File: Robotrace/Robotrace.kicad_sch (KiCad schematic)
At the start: 36 parts, among them J1 USB_C_Receptacle_USB2.0_16P, J10 Side_L, J6 STDC14, J7 Conn_02x05_Odd_Even, J8 Conn_02x05_Odd_Even, J9 Side_R, Q5 BSS138, SW1 SW_DPDT_x2, U1 STM32F469VGTx, Y1 8MHz

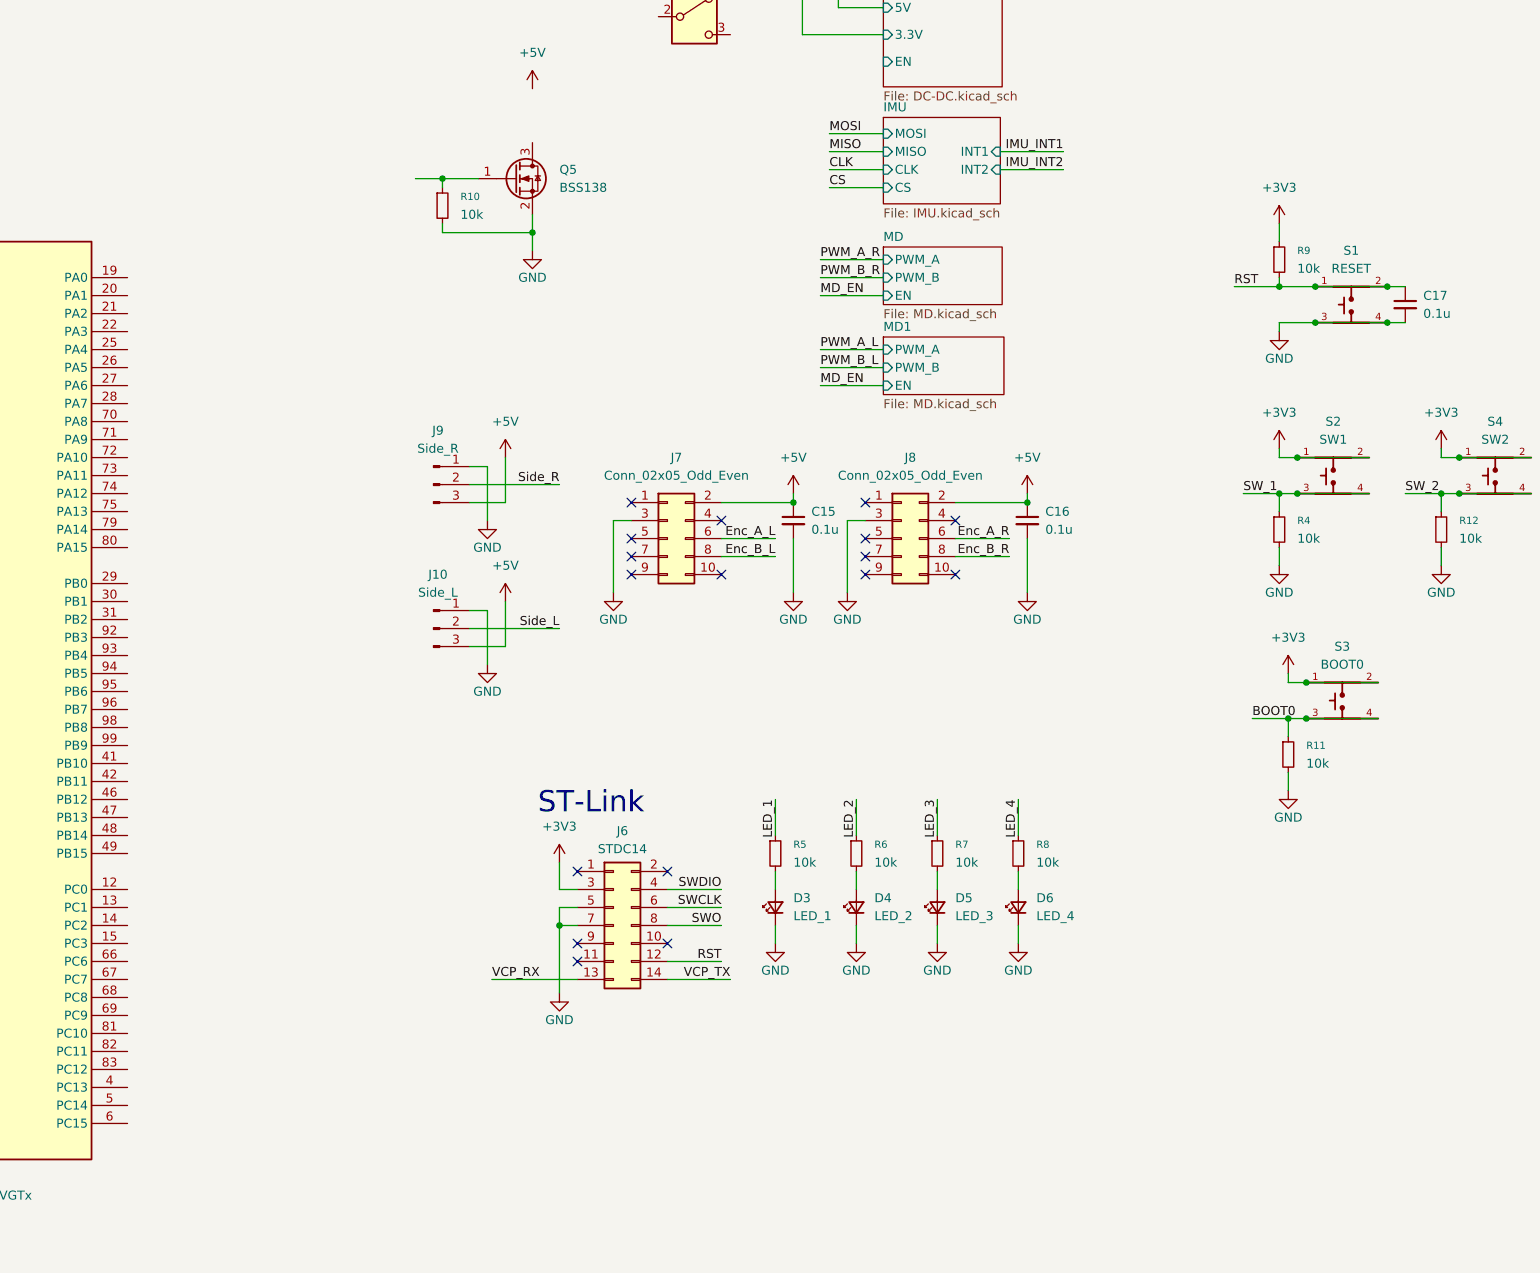
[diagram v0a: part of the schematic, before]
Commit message: STM32のGPIOにUSB/UART/SPI/ADCの配線を追加、J11にラインセンサーを接続
MCUのPA9-PA12(UART/USB), PB12-15(SPI)と、ADC用にPA0-7/PB0-1/PC0-3をラインセンサー13本+電圧監視1本に割り当て、J11コネクタのPin1-13にもラインセンサーの配線を追加。あわせてLineシートとCD74HC4067ライブラリを取り込み。

Co-Authored-By: Claude Sonnet 5 <noreply@anthropic.com>
Claude-Session: https://claude.ai/code/session_01781fWTRjWjmRZVNFFPgVZP
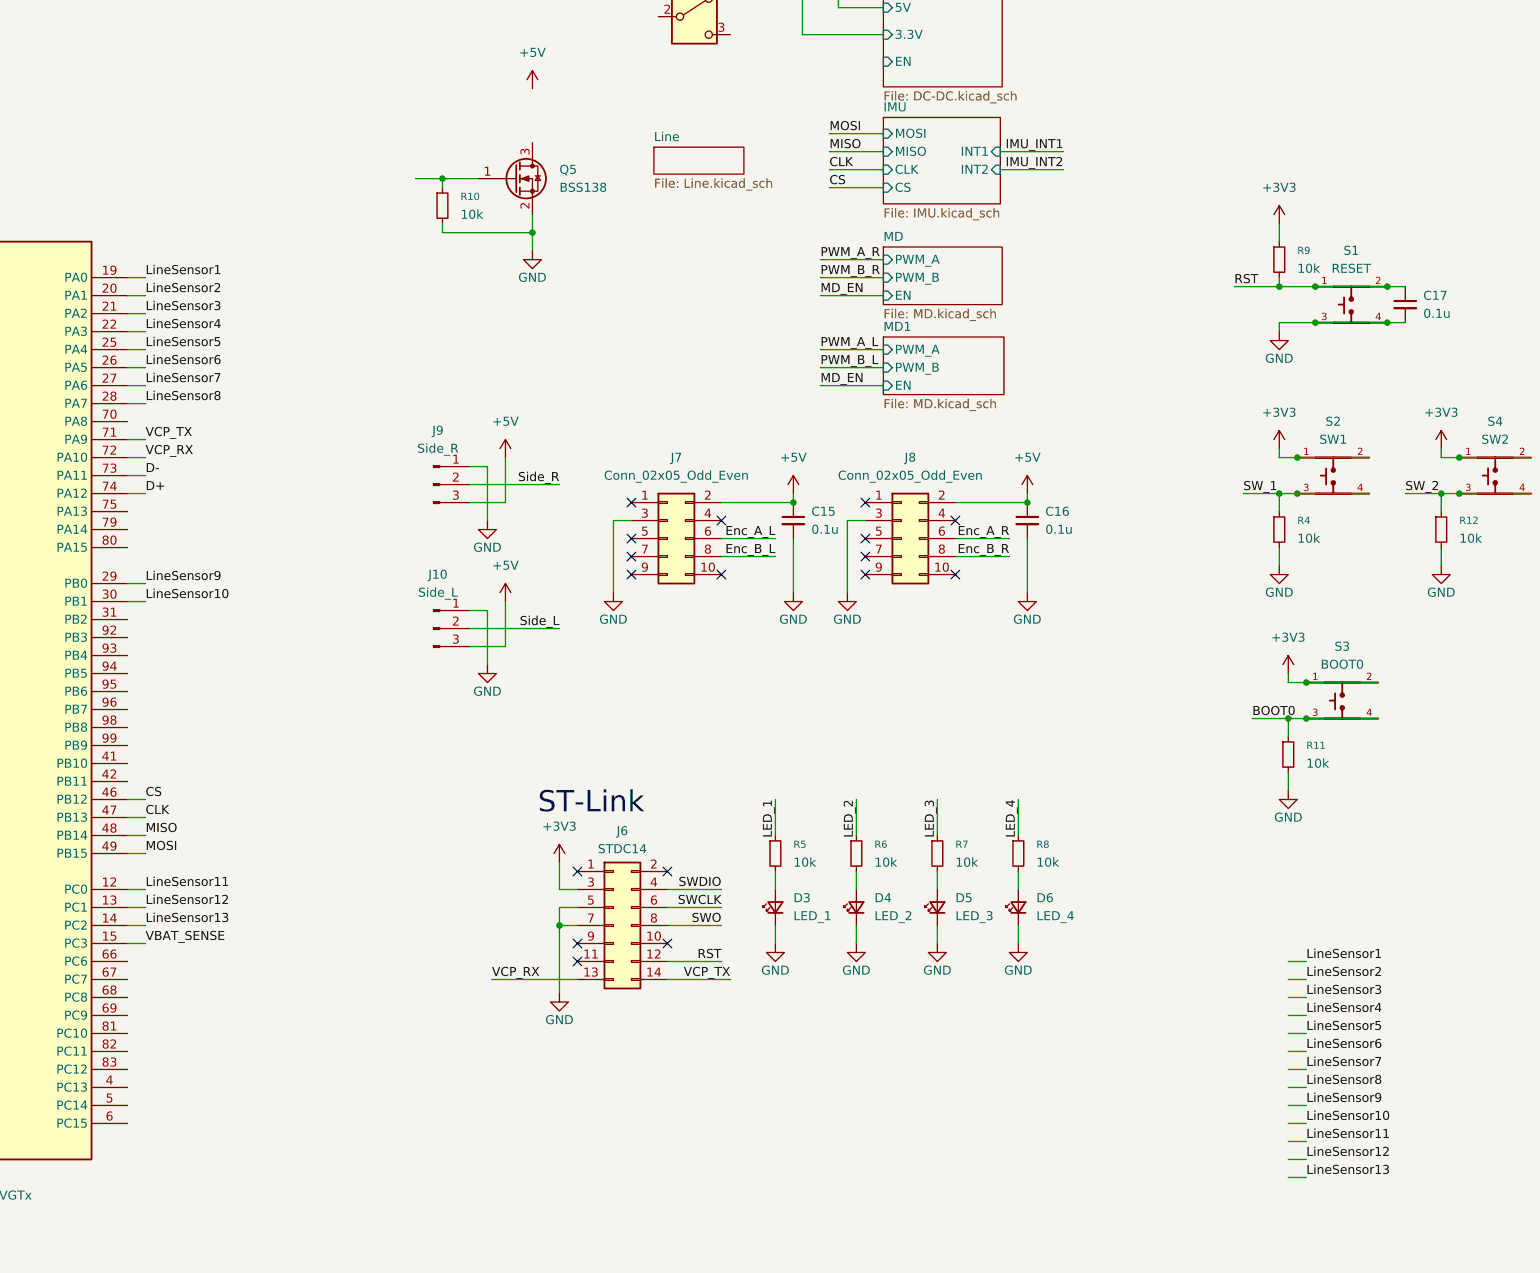
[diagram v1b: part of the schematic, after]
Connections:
- net CLK: now also U1.47 (PB13)
- net CS: now also U1.46 (PB12)
- net D+: now also U1.74 (PA12)
- net D-: now also U1.73 (PA11)
- net MISO: now also U1.48 (PB14)
- net MOSI: now also U1.49 (PB15)
- net VCP_RX: now also U1.72 (PA10)
- net VCP_TX: now also U1.71 (PA9)
- net LineSensor11: now reaches U1.12 (PC0)
- net LineSensor12: now reaches U1.13 (PC1)
- net LineSensor13: now reaches U1.14 (PC2)
- net VBAT_SENSE: now reaches U1.15 (PC3)
- net LineSensor1: now reaches U1.19 (PA0)
- net LineSensor2: now reaches U1.20 (PA1)
- net LineSensor3: now reaches U1.21 (PA2)
- net LineSensor4: now reaches U1.22 (PA3)
- net LineSensor5: now reaches U1.25 (PA4)
- net LineSensor6: now reaches U1.26 (PA5)
- net LineSensor7: now reaches U1.27 (PA6)
- net LineSensor8: now reaches U1.28 (PA7)
- net LineSensor9: now reaches U1.29 (PB0)
- net LineSensor10: now reaches U1.30 (PB1)
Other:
- added sheet Line (Line.kicad_sch)

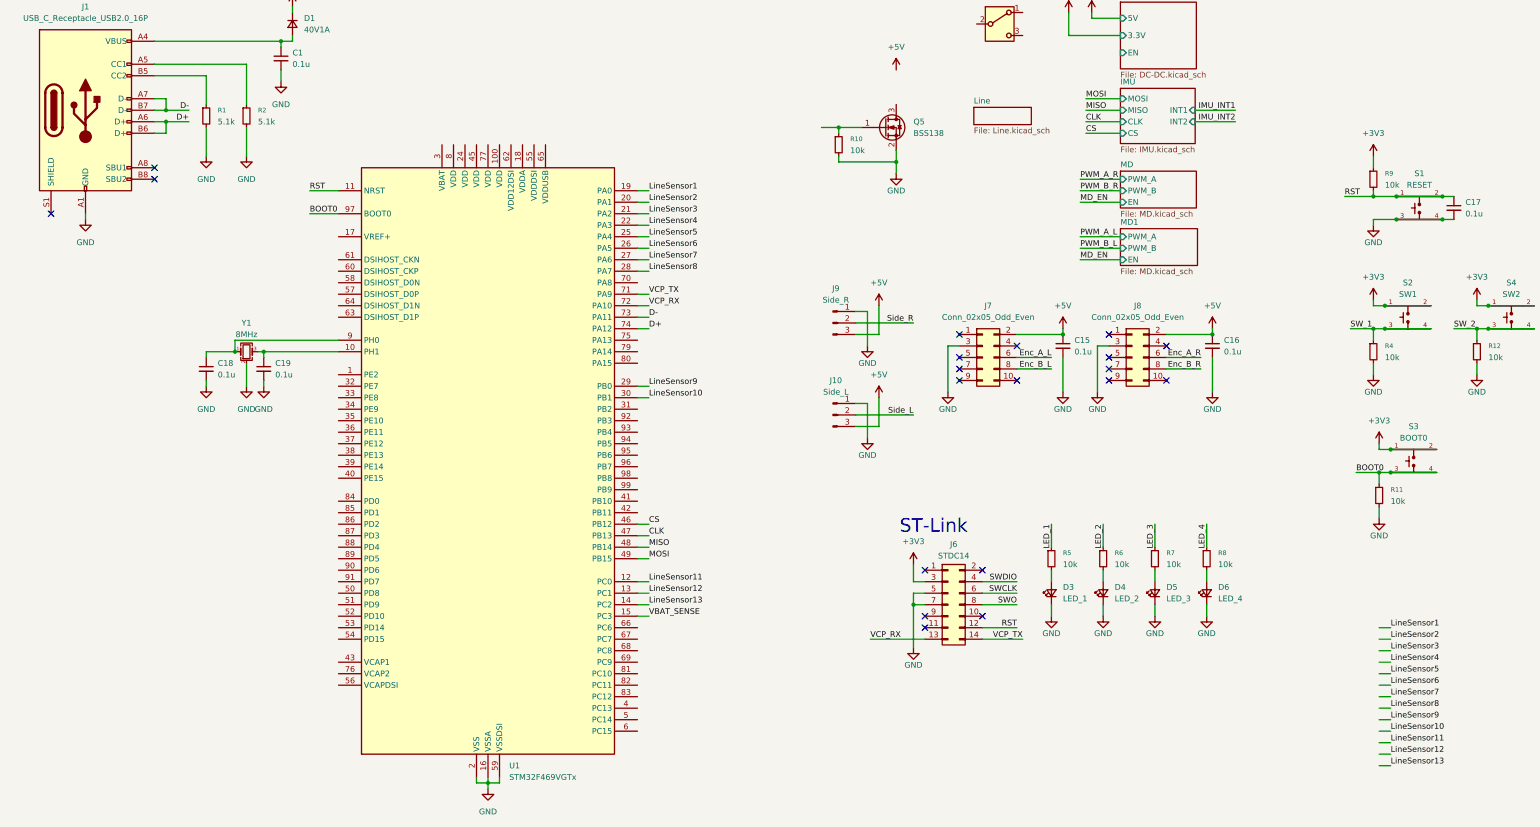
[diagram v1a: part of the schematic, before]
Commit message: モーターPWM/エンコーダ配線とST-LINK(SWD)配線を追加、J11欠落を修正
PA8/PB8/PB9/PC9をPWM_A_L/B_L/A_R/B_Rに、PB4/PB5/PC6/PC7をEnc_A_L/B_L/A_R/B_Rに割り当てて配線。PA13/PA14/PB3をSWDIO/SWCLK/SWOラベルに接続しST-LINK経由のデバッグを可能に(NRSTは既存のRSTラベル経由で接続済みだったため対応不要)。
また前回のトラブル対応(git checkout)で誤って失われていたJ11コネクタの復旧を反映(ユーザーがKiCad上で再配線)。

Co-Authored-By: Claude Sonnet 5 <noreply@anthropic.com>
Claude-Session: https://claude.ai/code/session_01781fWTRjWjmRZVNFFPgVZP
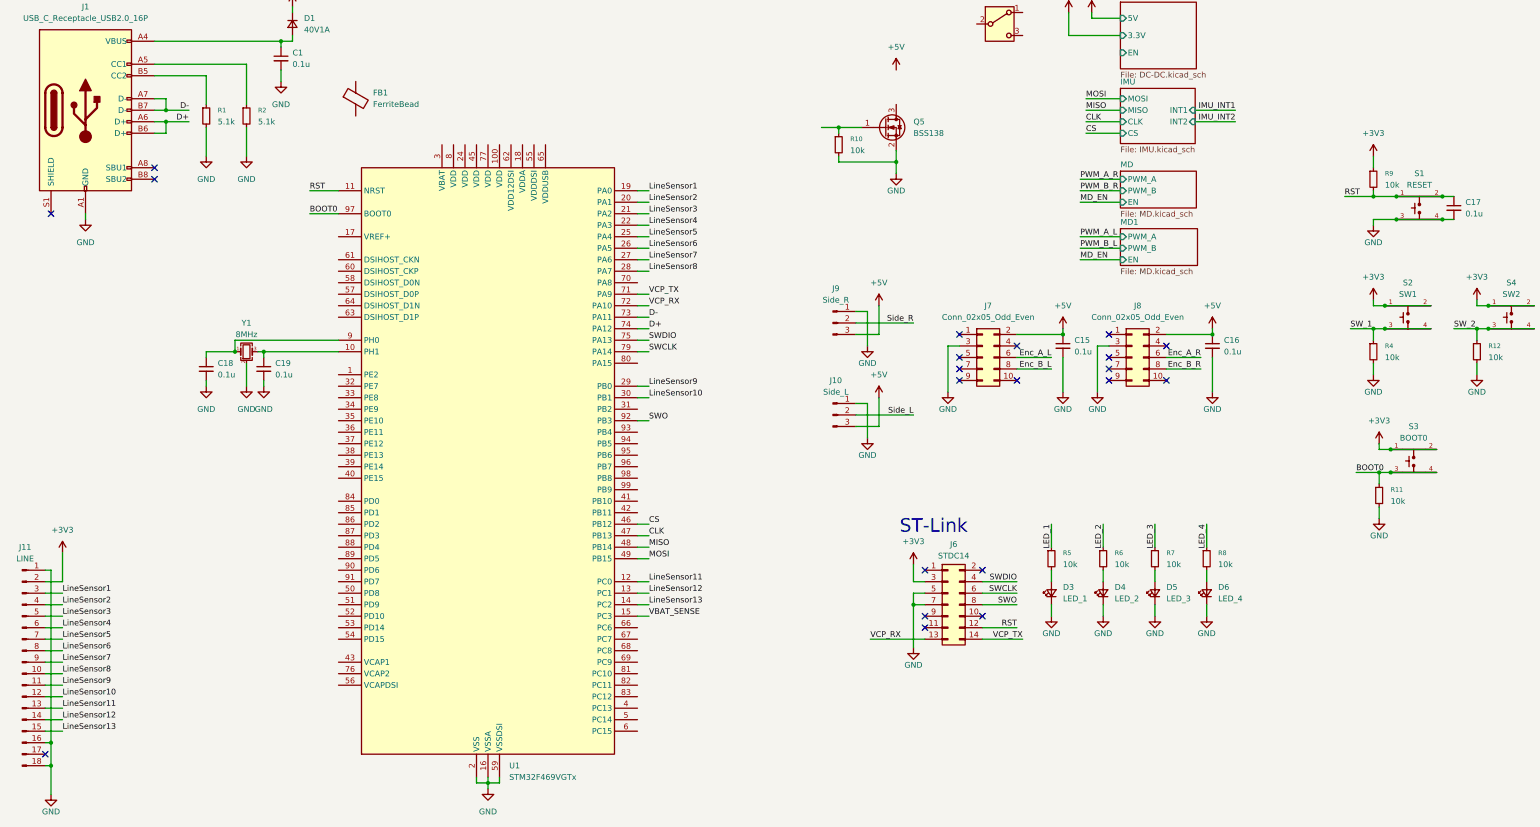
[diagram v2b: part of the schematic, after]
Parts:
- added FB1: FerriteBead, symbol Device:FerriteBead
- added J11: LINE, symbol Connector:Conn_01x18_Pin
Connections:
- net +3V3: now also J11.2 (Pin_2)
- net GND: now also J11.1 (Pin_1), J11.16 (Pin_16), J11.18 (Pin_18)
- net LineSensor1: now also J11.3 (Pin_3)
- net LineSensor10: now also J11.12 (Pin_12)
- net LineSensor11: now also J11.13 (Pin_13)
- net LineSensor12: now also J11.14 (Pin_14)
- net LineSensor13: now also J11.15 (Pin_15)
- net LineSensor2: now also J11.4 (Pin_4)
- net LineSensor3: now also J11.5 (Pin_5)
- net LineSensor4: now also J11.6 (Pin_6)
- net LineSensor5: now also J11.7 (Pin_7)
- net LineSensor6: now also J11.8 (Pin_8)
- net LineSensor7: now also J11.9 (Pin_9)
- net LineSensor8: now also J11.10 (Pin_10)
- net LineSensor9: now also J11.11 (Pin_11)
- net SWCLK: now also U1.79 (PA14)
- net SWDIO: now also U1.75 (PA13)
- net SWO: now also U1.92 (PB3)
- no-connect marks 20 -> 21
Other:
- removed sheet Line

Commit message: サイドセンサ・MDのEN・ビープ・LED・スイッチをMCUに配線
PA15->LED_1, PB2->LED_2, PB6->LED_3, PB10->LED_4, PB11->SW_1, PC8->SW_2,
PC10->MD_EN(2基のモータードライバ共通イネーブル), PC11->Side_L, PC12->Side_R, PC13->beep を割り当て。

Co-Authored-By: Claude Sonnet 5 <noreply@anthropic.com>
Claude-Session: https://claude.ai/code/session_01781fWTRjWjmRZVNFFPgVZP
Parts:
- added BZ1: Buzzer, symbol Device:Buzzer
- added C20, C21, C24, C36: 2.2u, Capacitor_SMD:C_0402_1005Metric, symbol Device:C_Small
- added C25, C26, C27, C28, C29, C30, C31, C32, C33, C34, C35: 0.1u, Capacitor_SMD:C_0402_1005Metric, symbol Device:C_Small
- added FB2: FerriteBead, symbol Device:FerriteBead
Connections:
- net +3V3: now also FB1.1, U1.100 (VDD), U1.24 (VDD), U1.3 (VBAT), U1.45 (VDD), U1.55 (VDDDSI), U1.77 (VDD), U1.8 (VDD), C27.1, C28.1, C29.1, C30.1, C31.1, C32.1, C33.1, C34.1, C36.1, FB2.2
- net +5V: now also BZ1.1 (+)
- net GND: now also C20.2, C21.2, C24.2, C25.2, C26.2, C27.2, C28.2, C29.2, C30.2, C31.2, C32.2, C33.2, C34.2, C35.2, C36.2
- net LED_1: now also U1.80 (PA15)
- net LED_2: now also U1.31 (PB2)
- net LED_3: now also U1.95 (PB6)
- net LED_4: now also U1.41 (PB10)
- net MD_EN: now also U1.81 (PC10)
- net SW_1: now also U1.42 (PB11)
- net SW_2: now also U1.68 (PC8)
- net Side_L: now also U1.82 (PC11)
- net Side_R: now also U1.83 (PC12)
- net +3.3VA: now reaches U1.17 (VREF+)
- net +3.3VA: now also FB1.2, U1.18 (VDDA), C26.1, C35.1
- net beep: now reaches U1.4 (PC13)
- net beep: now also Q5.1 (G), R10.1
- net at U1.43 (VCAP1): now also C20.1
- net DSI: now reaches U1.56 (VCAPDSI)
- net DSI: now also U1.62 (VDD12DSI), C24.1
- net at U1.65 (VDDUSB): now also C25.1, FB2.1
- net at U1.76 (VCAP2): now also C21.1
- net at Q5.3 (D): now also BZ1.2 (-)
- no-connect marks 21 -> 27
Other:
- moved on the sheet: C17, FB1, Q5, R10, R11, R12, R4, R9, S1, S2, S3, S4

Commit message: ビープをPWM出力可能なPB11(TIM2_CH4)に変更、SW_1はPC13に移動
PC13にはタイマー機能がないため、ビープをTIM2_CH4対応のPB11に付け替え、押し出されたSW_1をPC13(デジタル入力のみで良い)に割り当て直した。

Co-Authored-By: Claude Sonnet 5 <noreply@anthropic.com>
Claude-Session: https://claude.ai/code/session_01781fWTRjWjmRZVNFFPgVZP
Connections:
- net SW_1: now also U1.4 (PC13); no longer U1.42 (PB11)
- net beep: now also U1.42 (PB11); no longer U1.4 (PC13)
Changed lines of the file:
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@@
 		)
 	)
-	(label "SW_1"
+	(label "beep"
 		(at 152.4 130.81 0)
 		(effects
@@
 		)
 	)
-	(label "beep"
+	(label "SW_1"
 		(at 152.4 173.99 0)
 		(effects

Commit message: 水晶をFA-238V 12MHzに変更し、負荷容量C18/C19を15pFに修正
Y1をSG-210STF(アクティブ発振器、案として検討したが不採用)ではなくFA-238V 12.000000MHz(パッシブ水晶、CL=10pF)に確定。
それに伴い負荷容量として使うC18/C19を、誤って0.1uF(100nF)になっていたものから適正な15pFへ修正(2×CL-基板浮遊容量の目安で算出)。

Co-Authored-By: Claude Sonnet 5 <noreply@anthropic.com>
Claude-Session: https://claude.ai/code/session_01781fWTRjWjmRZVNFFPgVZP
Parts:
- C18, C19: value 0.1u -> 15pF
- Y1: value 8MHz -> FA-238V 12.000000MHz
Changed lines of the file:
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@@
 			)
 		)
-		(property "Value" "0.1u"
+		(property "Value" "15pF"
 			(at 69.85 100.3362 0)
 			(effects
@@
 			)
 		)
-		(property "Value" "8MHz"
+		(property "Value" "FA-238V 12.000000MHz"
 			(at 63.5 91.44 0)
 			(effects
@@
 			)
 		)
-		(property "Value" "0.1u"
+		(property "Value" "15pF"
 			(at 57.15 100.3362 0)
 			(effects
